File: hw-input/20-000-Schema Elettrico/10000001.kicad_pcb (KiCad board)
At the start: 4 copper layers, 45.7 x 32 mm, 37 parts, among them IC1 TLP291, IC2 TLP291, P1 CONN_4, P2 CONN_4, P3 CONN_4, P4 CONN_4, P5 CONN_4, P6 CONN_4, P7 CONN_4, P8 CONN_4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

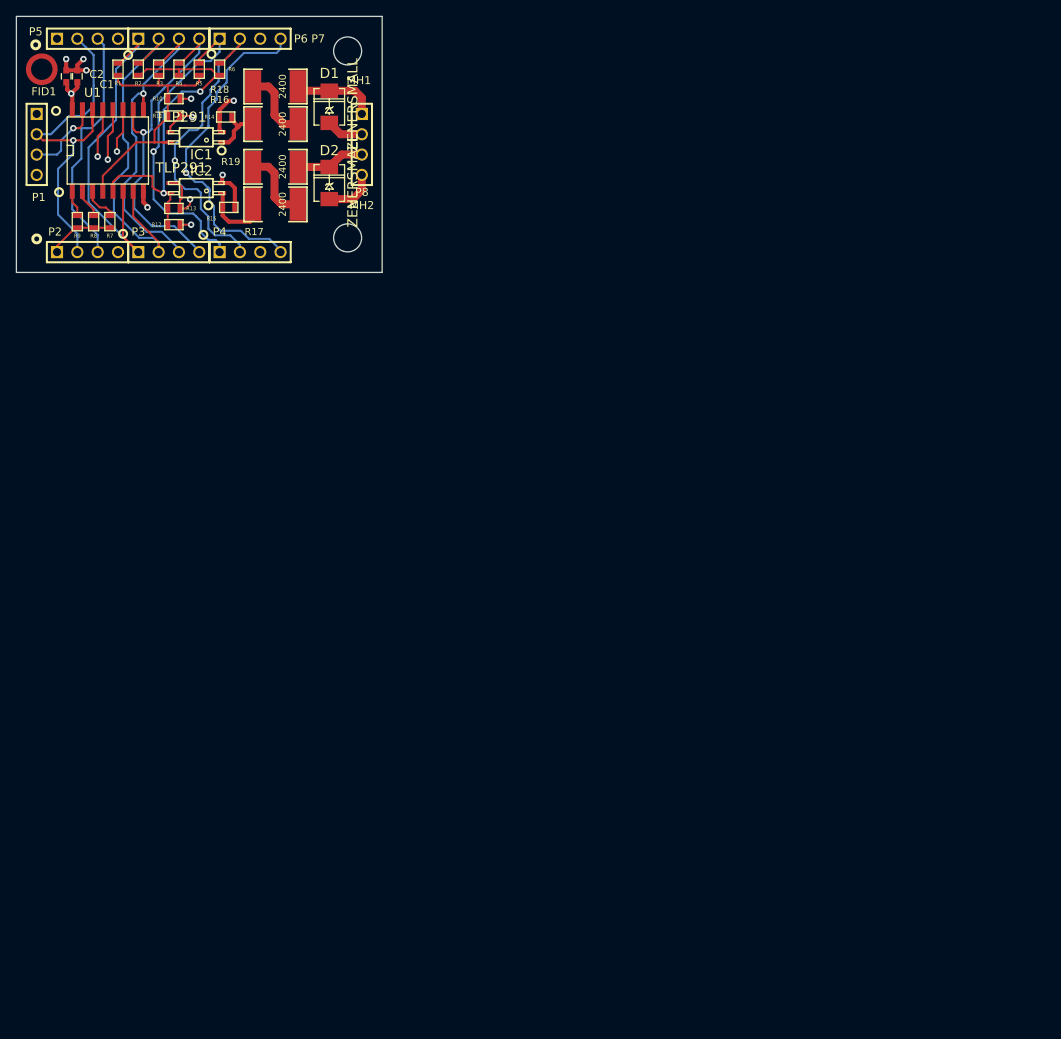
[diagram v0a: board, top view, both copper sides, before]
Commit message: Completato schema elettrico con codice produttore
Signed-off-by: CrazyDiamond <crazyd14@gmail.com>
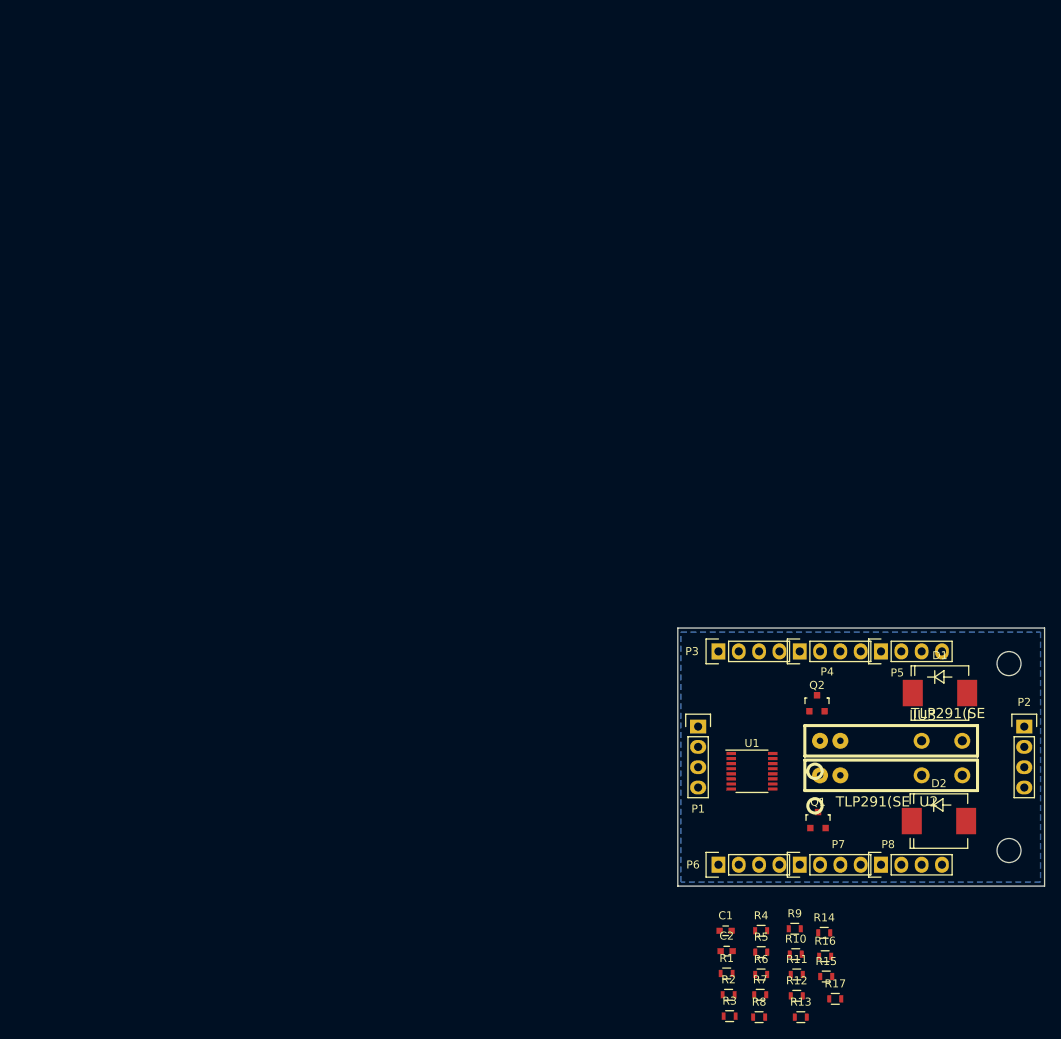
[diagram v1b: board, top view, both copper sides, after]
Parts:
- removed FID1: Fiducial_Modern_CopperTop, Fiducials:Fiducial_Modern_CopperTop
- removed IC1, IC2: TLP291, optocoupler-2-MINI-FLAT-4
- removed MH1, MH2: MountingHole_3-5mm, Mounting_Holes:MountingHole_3-5mm
- removed R18, R19: 2400, SM2512
- added Q1: Q_PMOS_GSD_BSS84, TO_SOT_Packages_SMD:SOT-23, F.Cu at (184.0, 143.4)
- added Q2: Q_PMOS_GSD_BSS84, TO_SOT_Packages_SMD:SOT-23, F.Cu at (183.9, 128.8)
- added REF**: MountingHole_3mm, Mounting_Holes:MountingHole_3mm, F.Cu at (207.9, 123.8)
- added REF**: MountingHole_3mm, Mounting_Holes:MountingHole_3mm, F.Cu at (207.9, 147.2)
- added U2: TLP291(SE, os_photomos:AQZ-SIL-4, F.Cu at (182.4, 135.9)
- added U3: TLP291(SE, os_photomos:AQZ-SIL-4, F.Cu at (182.4, 131.6)
- C1: value 100n -> C_100n_0603_10_X7R_25V
- C2: value 1u -> C_1u_0603_10_X7R_25V
- D1, D2: value ZENERSMALL -> TVS_SMC_49.1V; footprint DO214 -> Diodes_SMD:SMC_Standard
- P1, P2, P3, P4, P5, P6, P7, P8: value CONN_4 -> PLUG_01X04_254; footprint PIN_ARRAY_4x1 -> Socket_Strips:Socket_Strip_Straight_1x04
- R1, R2, R3, R4, R5, R6: value 0 -> R_0_0603_5; footprint SM0603 -> Resistors_SMD:R_0603
- R10, R12: value 1000 -> R_1K_0603_5; footprint SM0603 -> Resistors_SMD:R_0603
- R11, R13, R7, R8, R9: value 10000 -> R_10K_0603_5; footprint SM0603 -> Resistors_SMD:R_0603
- R14, R15: footprint SM0603 -> Resistors_SMD:R_0603
- R16, R17: footprint SM2512 -> Resistors_SMD:R_0603
- U1: value PCF8574 -> TCA9554; footprint SO16L -> Housings_SSOP:SSOP-16_3.9x4.9mm_Pitch0.635mm
- moved R3 138.2 mm to (173.0, 167.9), turned to 0 degrees
- moved R2 137.2 mm to (172.8, 165.2), turned to 0 degrees
- moved C2 137.0 mm to (172.6, 159.8), turned to 0 degrees
- moved R1 136.3 mm to (172.6, 162.6), turned to 0 degrees
- moved C1 134.1 mm to (172.5, 157.2), turned to 0 degrees
- moved R11 132.6 mm to (181.4, 162.7)
- moved R10 132.2 mm to (181.2, 160.1), turned to 0 degrees
- moved R6 131.9 mm to (176.9, 162.7), turned to 0 degrees
- moved P2 131.3 mm to (209.8, 131.7), turned to 270 degrees
- moved R5 130.8 mm to (176.9, 159.9), turned to 0 degrees
- moved R4 130.0 mm to (176.9, 157.2), turned to 0 degrees
- moved R8 129.6 mm to (176.7, 168.0), turned to 0 degrees
- moved R13 127.9 mm to (181.9, 168.0)
- moved R14 126.5 mm to (184.8, 157.5)
- moved R7 126.3 mm to (176.8, 165.2), turned to 0 degrees
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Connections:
- C1 pad 1: VDD -> +5V
- C2 pad 1: VDD -> +5V
- D1 pad 1: /IO_0_N -> /IO_0_P
- D1 pad 2: /IO_0_P -> /IO_0_N
- D2 pad 1: /IO_1_N -> /IO_1_P
- D2 pad 2: /IO_1_P -> /IO_1_N
- P1 pad 1: VDD -> +5V
- P2 pad 1: VDD -> /IO_0_P
- P2 pad 2: /I2C_SCL -> /IO_0_N
- P2 pad 3: /I2C_SDA -> /IO_1_P
- P2 pad 4: GND -> /IO_1_N
- P3 pad 1: /IO_2_CMD -> +5V
- P3 pad 2: /IO_3_CMD -> /I2C_SCL
- P3 pad 3: /IO_4_CMD -> /I2C_SDA
- P3 pad 4: /IO_5_CMD -> GND
- P4 pad 1: /IO_6_CMD -> /IO_2_CMD
- P4 pad 2: /IO_7_CMD -> /IO_3_CMD
- P4 pad 3: Net-(P4-Pad3) -> /IO_4_CMD
- P4 pad 4: /I2C_INT -> /IO_5_CMD
- P5 pad 1: VDD -> /IO_6_CMD
- P5 pad 2: /I2C_SCL -> /IO_7_CMD
- P5 pad 3: /I2C_SDA -> Net-(P5-Pad3)
- P5 pad 4: GND -> /I2C_INT
- P6 pad 1: /IO_2_CMD -> +5V
- P6 pad 2: /IO_3_CMD -> /I2C_SCL
- P6 pad 3: /IO_4_CMD -> /I2C_SDA
- P6 pad 4: /IO_5_CMD -> GND
- P7 pad 1: /IO_6_CMD -> /IO_2_CMD
- P7 pad 2: /IO_7_CMD -> /IO_3_CMD
- P7 pad 3: Net-(P7-Pad3) -> /IO_4_CMD
- P7 pad 4: /I2C_INT -> /IO_5_CMD
- P8 pad 1: /IO_0_P -> /IO_6_CMD
- P8 pad 2: /IO_0_N -> /IO_7_CMD
- P8 pad 3: /IO_1_P -> Net-(P8-Pad3)
- P8 pad 4: /IO_1_N -> /I2C_INT
- R1 pad 1: /IO_2_CMD -> /IO_0_CMD
- R1 pad 2: /IO_0_CMD -> /IO_2_CMD
- R10 pad 1: VDD -> +5V
- R12 pad 1: VDD -> +5V
- R2 pad 1: /IO_3_CMD -> /IO_1_CMD
- R2 pad 2: /IO_1_CMD -> /IO_3_CMD
- R3 pad 1: /IO_4_CMD -> /IO_0_CMD
- R3 pad 2: /IO_0_CMD -> /IO_4_CMD
- R4 pad 1: /IO_5_CMD -> /IO_1_CMD
- R4 pad 2: /IO_1_CMD -> /IO_5_CMD
- R5 pad 1: /IO_6_CMD -> /IO_0_CMD
- R5 pad 2: /IO_0_CMD -> /IO_6_CMD
- R6 pad 1: /IO_7_CMD -> /IO_1_CMD
- R6 pad 2: /IO_1_CMD -> /IO_7_CMD
- R7 pad 1: VDD -> +5V
- R8 pad 1: VDD -> +5V
- R9 pad 1: VDD -> +5V
- U1 pad 16: VDD -> +5V
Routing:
- net /I2C_INT: track 62.1 -> 0.00 mm, vias 2 -> 0
- net /IO_7_CMD: track 54.4 -> 0.00 mm, vias 2 -> 0
- net /IO_6_CMD: track 52.1 -> 0.00 mm, vias 2 -> 0
- net /IO_2_CMD: track 48.2 -> 0.00 mm
- net /I2C_SCL: track 47.6 -> 0.00 mm, vias 1 -> 0
- net /IO_3_CMD: track 46.8 -> 0.00 mm
- net /IO_1_CMD: track 45.3 -> 0.00 mm, vias 2 -> 0
- net /IO_5_CMD: track 43.8 -> 0.00 mm, vias 1 -> 0
- net /IO_4_CMD: track 42.2 -> 0.00 mm, vias 1 -> 0
- net /I2C_SDA: track 41.8 -> 1.65 mm, vias 1 -> 0
- net /IO_0_CMD: track 34.2 -> 0.00 mm
- net /IO_1_N: track 29.3 -> 0.00 mm, vias 1 -> 0
- net /IO_0_N: track 27.6 -> 0.00 mm, vias 1 -> 0
- net GND: track 19.7 -> 0.00 mm, vias 6 -> 0
- net VDD: track 16.6 -> 0.00 mm, vias 3 -> 0
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- added copper zone on In1.Cu, net +5V
- added copper zone on B.Cu, net GND
- removed copper zone on GND, net GND
- removed copper zone on VCC, net VDD
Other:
- board size 45.7 x 32 mm -> 45.8 x 32.3 mm
- net class Default: clearance 0.254 -> 0.2; trace_width 0.127 -> 0.25; via_dia 0.8001 -> 0.6; via_drill 0.50038 -> 0.4
- rule pad_to_mask_clearance: 0.254 -> 0.2
- rule trace_clearance: 0.254 -> 0.2
- rule trace_min: 0.127 -> 0.2
- rule via_min_drill: 0.50038 -> 0.3
- rule via_min_size: 0.8001 -> 0.4

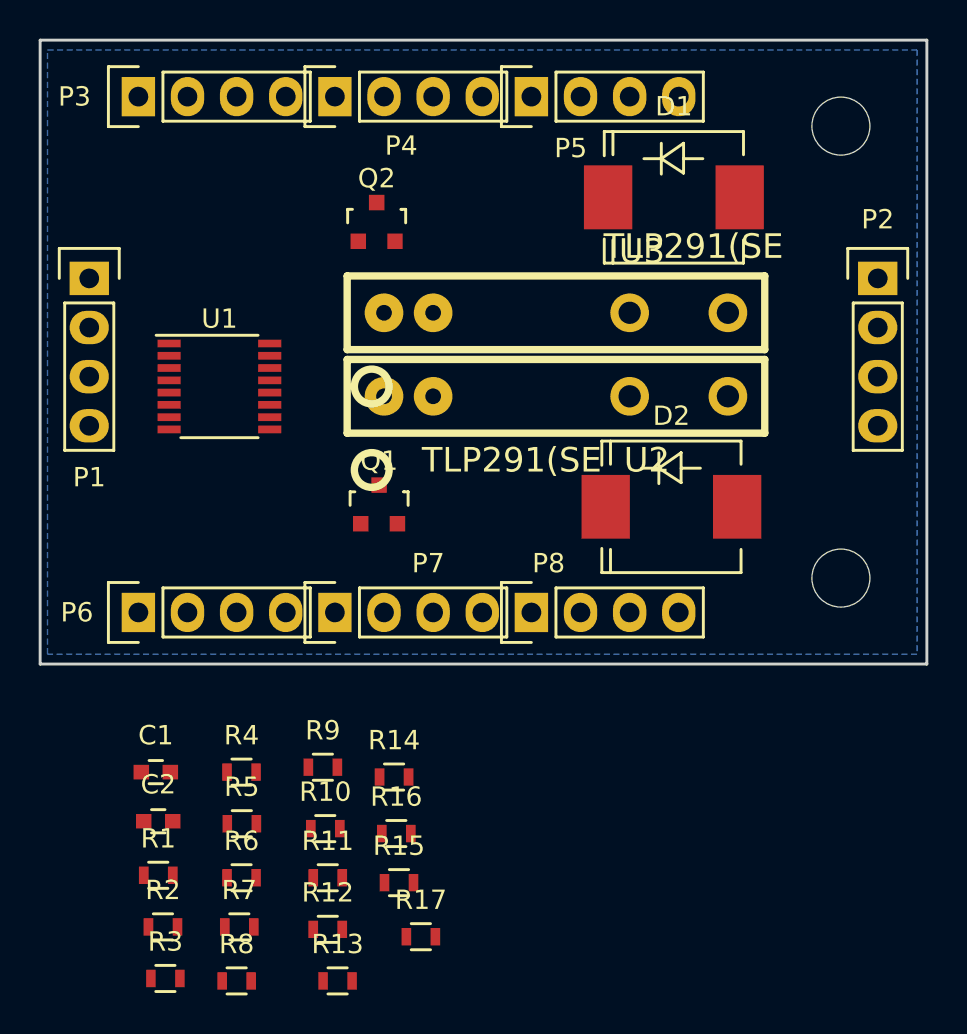
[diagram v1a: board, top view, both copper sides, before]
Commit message: completato schema elettrico e sbroglio
Signed-off-by: CrazyDiamond <crazyd14@gmail.com>
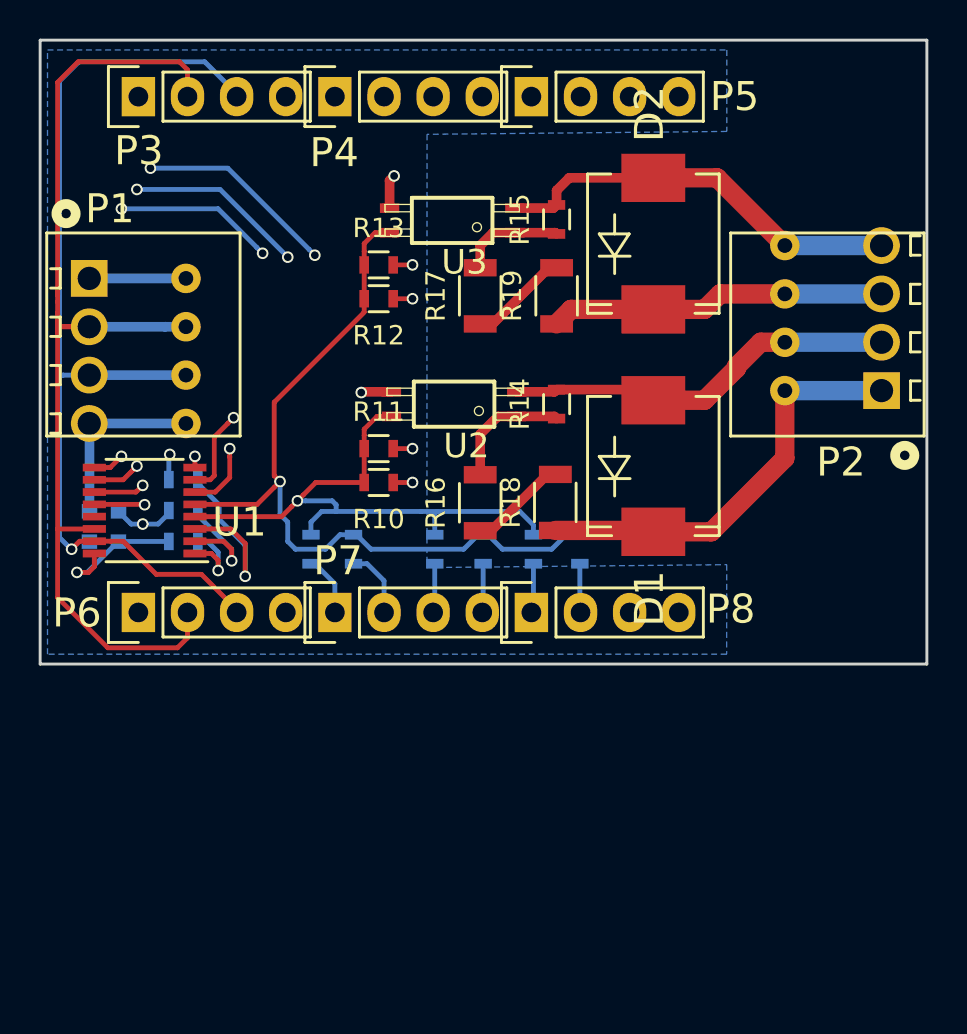
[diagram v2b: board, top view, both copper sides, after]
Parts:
- removed Q1, Q2: Q_PMOS_GSD_BSS84, TO_SOT_Packages_SMD:SOT-23
- removed REF** (x2): MountingHole_3mm, Mounting_Holes:MountingHole_3mm
- added R18: R_2K4_1206_5, Resistors_SMD:R_1206, F.Cu at (193.1, 143.3)
- added R19: R_2K4_1206_5, Resistors_SMD:R_1206, F.Cu at (193.2, 132.6)
- C1, C2, R1, R2, R3, R4, R5, R6, R7, R8, R9: moved to B.Cu
- P1, P2: value PLUG_01X04_254 -> TERMINAL_01X04_250_RA_SPRING; footprint Socket_Strips:Socket_Strip_Straight_1x04 -> os_terminal_block:1770908
- R14, R15: value 100 -> R_100_0603_5
- R16, R17: value 2400 -> R_2K4_1206_5; footprint Resistors_SMD:R_0603 -> Resistors_SMD:R_1206
- U2, U3: footprint os_photomos:AQZ-SIL-4 -> os_optocoupler:TLP291
- moved R13 37.1 mm to (184.0, 131.0)
- moved R15 35.2 mm to (193.2, 128.7), turned to 90 degrees
- moved R17 33.3 mm to (189.2, 132.6), turned to 90 degrees
- moved R12 32.7 mm to (184.0, 132.8), turned to 180 degrees
- moved R3 26.2 mm to (186.9, 145.7), turned to 270 degrees
- moved R8 24.5 mm to (173.9, 143.7)
- moved R6 24.4 mm to (194.4, 145.7), turned to 270 degrees
- moved R7 23.3 mm to (173.9, 142.1)
- moved R11 22.3 mm to (184.0, 140.5)
- moved R2 21.9 mm to (182.7, 145.7), turned to 270 degrees
- moved R14 21.0 mm to (193.2, 138.2), turned to 90 degrees
- moved R5 20.7 mm to (192.0, 145.7), turned to 270 degrees
- moved R1 18.6 mm to (180.5, 145.7), turned to 270 degrees
- moved R10 18.1 mm to (184.0, 142.2), turned to 180 degrees
- moved R16 17.6 mm to (189.2, 143.3), turned to 90 degrees
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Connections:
- P5 pad 3: Net-(P5-Pad3) -> (no net)
- P8 pad 3: Net-(P8-Pad3) -> (no net)
- R14 pad 1: /IO_0_N -> Net-(R14-Pad1)
- R14 pad 2: Net-(R14-Pad2) -> /IO_0_N
- R15 pad 1: /IO_1_N -> Net-(R15-Pad1)
- R15 pad 2: Net-(R15-Pad2) -> /IO_1_N
- R16 pad 1: Net-(R14-Pad2) -> Net-(R16-Pad1)
- R16 pad 2: Net-(R16-Pad2) -> Net-(R14-Pad1)
- R17 pad 1: Net-(R15-Pad2) -> Net-(R17-Pad1)
- R17 pad 2: Net-(R17-Pad2) -> Net-(R15-Pad1)
- U2 pad 1: Net-(R14-Pad2) -> Net-(R14-Pad1)
- U3 pad 1: Net-(R15-Pad2) -> Net-(R15-Pad1)
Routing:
- net /IO_7_CMD: track 0.00 -> 85.2 mm, vias 0 -> 1
- net /IO_6_CMD: track 0.00 -> 72.4 mm, vias 0 -> 3
- net /IO_5_CMD: track 0.00 -> 66.7 mm, vias 0 -> 3
- net /IO_4_CMD: track 0.00 -> 59.9 mm, vias 0 -> 3
- net /I2C_SCL: track 0.00 -> 55.7 mm
- net /I2C_SDA: track 1.65 -> 53.5 mm, vias 0 -> 1
- net /IO_3_CMD: track 0.00 -> 43.0 mm, vias 0 -> 1
- net /IO_1_CMD: track 0.00 -> 40.9 mm, vias 0 -> 1
- net /IO_2_CMD: track 0.00 -> 39.4 mm, vias 0 -> 1
- net /IO_0_CMD: track 0.00 -> 30.8 mm, vias 0 -> 1
- net /IO_0_P: track 0.00 -> 22.0 mm
- net /IO_1_N: track 0.00 -> 21.5 mm
- net /IO_0_N: track 0.00 -> 20.4 mm
- net +5V: track 0.18 -> 20.2 mm, vias 0 -> 5
- net /IO_1_P: track 0.00 -> 17.4 mm
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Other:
- rule trace_min: 0.2 -> 0.1
